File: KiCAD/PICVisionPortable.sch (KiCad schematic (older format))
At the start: 43 parts, among them SW1 left, SW2 up, SW3 down, SW4 select, SW5 Power, SW6 right, SW7 Reset, U1 LD33V, U2 PIC24FJ64GA002

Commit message: adaptation de jeux
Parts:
- R12: value 150R -> 200R
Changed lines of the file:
@@
 P 6000 2700
 F 0 "R12" V 6080 2700 50  0000 C CNN
-F 1 "150R" V 6000 2700 50  0000 C CNN
+F 1 "200R" V 6000 2700 50  0000 C CNN
 F 2 "~" H 6000 2700 60  0000 C CNN
 F 3 "~" H 6000 2700 60  0000 C CNN

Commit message: ajout photos
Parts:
- added D1: 1N4001, symbol DIODE
- added RV1: 10K, symbol POT
- renumbered D1 to D2, SW5 to SW2, SW2 to SW3, SW3 to SW4, SW4 to SW5
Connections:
- net GND: now also RV1.3
- net Vlcd: now also R19.1, RV1.1; no longer U1.3 (Vin)
- net at LCD1.3 (Vo): now also RV1.2
- net at D2.1 (A): now also U1.3 (Vin), D1.2 (K); no longer SW2.3
- new net: D1.1 (A), SW2.3
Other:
- note added: "4,7V\n\n\n"
- note added: "GND\n"
- note added: "contrast\n"
- note removed: "5,3V\n\n\n"
- moved on the sheet: BT1, R18, SW2
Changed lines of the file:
@@
 encoding utf-8
 Sheet 1 1
-Title "CHIPCON portable"
+Title "PICVisionPortable"
 Date "26 jan 2015"
 Rev ""
@@
 L BATTERY BT1
 U 1 1 54BFE856
-P 1500 7050
-F 0 "BT1" H 1500 7250 50  0000 C CNN
-F 1 "4xAA" H 1500 6860 50  0000 C CNN
-F 2 "~" H 1500 7050 60  0000 C CNN
-F 3 "~" H 1500 7050 60  0000 C CNN
-	1    1500 7050
+P 1000 7050
+F 0 "BT1" H 1000 7250 50  0000 C CNN
+F 1 "4xAA" H 1000 6860 50  0000 C CNN
+F 2 "~" H 1000 7050 60  0000 C CNN
+F 3 "~" H 1000 7050 60  0000 C CNN
+	1    1000 7050
 	0    1    1    0
 $EndComp
 $Comp
-L SWITCH_INV SW5
+L SWITCH_INV SW2
 U 1 1 54BFE865
-P 2150 6750
-F 0 "SW5" H 1950 6900 50  0000 C CNN
-F 1 "Power" H 2000 6600 50  0000 C CNN
-F 2 "~" H 2150 6750 60  0000 C CNN
-F 3 "~" H 2150 6750 60  0000 C CNN
-	1    2150 6750
-	1    0    0    -1
-$EndComp
-Text Notes 1400 6650 0    60   ~ 0
+P 1650 6750
+F 0 "SW2" H 1450 6900 50  0000 C CNN
+F 1 "Power" H 1500 6600 50  0000 C CNN
+F 2 "~" H 1650 6750 60  0000 C CNN
+F 3 "~" H 1650 6750 60  0000 C CNN
+	1    1650 6750
+	1    0    0    -1
+$EndComp
+Text Notes 900  6650 0    60   ~ 0
 6V+
 $Comp
 L GND #PWR1
 U 1 1 54BFE879
-P 1500 7500
-F 0 "#PWR1" H 1500 7500 30  0001 C CNN
-F 1 "GND" H 1500 7430 30  0001 C CNN
-F 2 "~" H 1500 7500 60  0000 C CNN
-F 3 "~" H 1500 7500 60  0000 C CNN
-	1    1500 7500
-	1    0    0    -1
-$EndComp
-Text Notes 2250 7000 0    60   ~ 0
+P 1000 7500
+F 0 "#PWR1" H 1000 7500 30  0001 C CNN
+F 1 "GND" H 1000 7430 30  0001 C CNN
+F 2 "~" H 1000 7500 60  0000 C CNN
+F 3 "~" H 1000 7500 60  0000 C CNN
+	1    1000 7500
+	1    0    0    -1
+$EndComp
+Text Notes 1750 7000 0    60   ~ 0
 On
-Text Notes 2250 6550 0    60   ~ 0
+Text Notes 1750 6550 0    60   ~ 0
 Off
 $Comp
@@
 L R R18
 U 1 1 54BFF69E
-P 7750 2000
-F 0 "R18" V 7830 2000 50  0000 C CNN
-F 1 "10K" V 7750 2000 50  0000 C CNN
-F 2 "~" H 7750 2000 60  0000 C CNN
-F 3 "~" H 7750 2000 60  0000 C CNN
-	1    7750 2000
+P 7900 2000
+F 0 "R18" V 7980 2000 50  0000 C CNN
+F 1 "10K" V 7900 2000 50  0000 C CNN
+F 2 "~" H 7900 2000 60  0000 C CNN
+F 3 "~" H 7900 2000 60  0000 C CNN
+	1    7900 2000
 	1    0    0    -1
 $EndComp
@@
 $EndComp
 $Comp
-L SW_PUSH_SMALL SW3
+L SW_PUSH_SMALL SW4
 U 1 1 54C27F6B
 P 1850 2850
-F 0 "SW3" H 2000 2960 30  0000 C CNN
+F 0 "SW4" H 2000 2960 30  0000 C CNN
 F 1 "down" V 1850 2771 30  0000 C CNN
 F 2 "~" H 1850 2850 60  0000 C CNN
@@
 $EndComp
 $Comp
-L SW_PUSH_SMALL SW2
+L SW_PUSH_SMALL SW3
 U 1 1 54C27F81
 P 1850 2100
-F 0 "SW2" H 2000 2210 30  0000 C CNN
+F 0 "SW3" H 2000 2210 30  0000 C CNN
 F 1 "up" V 1850 2021 30  0000 C CNN
 F 2 "~" H 1850 2100 60  0000 C CNN
@@
 $EndComp
 $Comp
-L SW_PUSH_SMALL SW4
+L SW_PUSH_SMALL SW5
 U 1 1 54C27F87
 P 1850 3550
-F 0 "SW4" H 2000 3660 30  0000 C CNN
+F 0 "SW5" H 2000 3660 30  0000 C CNN
 F 1 "select" V 1850 3471 30  0000 C CNN
 F 2 "~" H 1850 3550 60  0000 C CNN
@@
 LCD_RST
 Wire Wire Line
-	1500 7350 1500 7500
-Wire Wire Line
-	1500 6750 1650 6750
+	1000 7350 1000 7500
+Wire Wire Line
+	1000 6750 1150 6750
 Wire Wire Line
 	3000 6200 3000 6300
@@
 Connection ~ 8150 2300
 Wire Wire Line
-	7750 2250 7750 2500
-Connection ~ 7750 2500
-Wire Wire Line
 	7250 2300 7250 2200
 Wire Wire Line
 	7050 2500 7050 2200
-Wire Wire Line
-	8300 1750 7750 1750
 Wire Wire Line
 	3200 7350 3200 7450
@@
 	3100 6850 3400 6850
 $Comp
-L DIODE D1
+L DIODE D2
 U 1 1 54F09C9E
 P 2900 6850
-F 0 "D1" H 2900 6950 50  0000 C CNN
+F 0 "D2" H 2900 6950 50  0000 C CNN
 F 1 "1N4001" H 2900 6750 50  0000 C CNN
 F 2 "" H 2900 6850 60  0000 C CNN
@@
 $EndComp
 Wire Wire Line
-	2650 6850 2700 6850
+	2150 6850 2200 6850
 Wire Wire Line
 	3200 6950 3200 6850
 Connection ~ 3200 6850
-Wire Wire Line
-	3100 6850 3100 6200
 Text Notes 3450 6950 0    60   ~ 0
-5,3V\n\n\n
+4,7V\n\n\n
 Text Notes 3100 7050 0    60   ~ 0
 +
@@
 Wire Wire Line
 	6000 6400 8000 6400
+$Comp
+L POT RV1
+U 1 1 551151C3
+P 8150 1400
+F 0 "RV1" H 8150 1300 50  0000 C CNN
+F 1 "10K" H 8150 1400 50  0000 C CNN
+F 2 "" H 8150 1400 60  0000 C CNN
+F 3 "" H 8150 1400 60  0000 C CNN
+	1    8150 1400
+	0    -1   -1   0
+$EndComp
+Wire Wire Line
+	8150 1650 8150 1750
+Connection ~ 8150 1750
+$Comp
+L GND #PWR15
+U 1 1 55115405
+P 8150 1100
+F 0 "#PWR15" H 8150 1100 30  0001 C CNN
+F 1 "GND" H 8150 1030 30  0001 C CNN
+F 2 "~" H 8150 1100 60  0000 C CNN
+F 3 "~" H 8150 1100 60  0000 C CNN
+	1    8150 1100
+	-1   0    0    1
+$EndComp
+Wire Wire Line
+	8150 1100 8150 1150
+Wire Wire Line
+	7900 2250 7900 2500
+Connection ~ 7900 2500
+Wire Wire Line
+	8300 1750 7900 1750
+Wire Wire Line
+	7350 2200 7350 2400
+Wire Wire Line
+	7350 2400 7750 2400
+Wire Wire Line
+	7750 2400 7750 1400
+Wire Wire Line
+	7750 1400 8000 1400
+Text Notes 8250 1300 0    60   ~ 0
+contrast\n
+Text Notes 8200 1050 0    60   ~ 0
+GND\n
+$Comp
+L DIODE D1
+U 1 1 55119C3F
+P 2400 6850
+F 0 "D1" H 2400 6950 50  0000 C CNN
+F 1 "1N4001" H 2400 6750 50  0000 C CNN
+F 2 "" H 2400 6850 60  0000 C CNN
+F 3 "" H 2400 6850 60  0000 C CNN
+	1    2400 6850
+	1    0    0    -1
+$EndComp
+Wire Wire Line
+	2600 6850 2700 6850
+Wire Wire Line
+	2700 6850 2700 6600
+Wire Wire Line
+	2700 6600 3100 6600
+Wire Wire Line
+	3100 6600 3100 6200
 $EndSCHEMATC

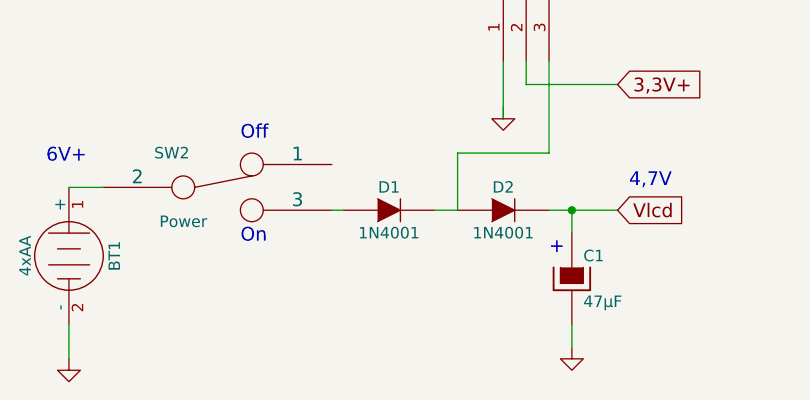
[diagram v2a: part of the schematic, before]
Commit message: added contrast potentiometer to schematic
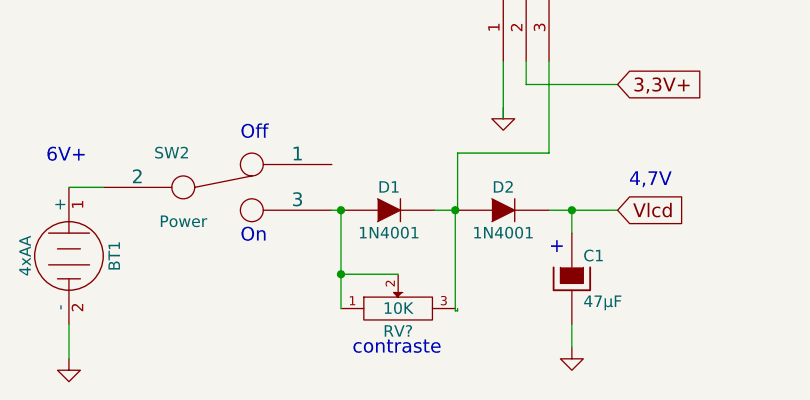
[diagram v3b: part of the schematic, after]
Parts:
- added RV?: 10K, symbol POT
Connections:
- wire segments 163 -> 168
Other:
- note added: "contraste"
